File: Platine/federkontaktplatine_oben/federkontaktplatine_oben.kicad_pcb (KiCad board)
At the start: 2 copper layers, 256 x 138 mm, 17 parts, among them J2 Conn_01x08

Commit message: Platinen überarbeitet
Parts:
- added H1: MountingHole, MountingHole:MountingHole_3.2mm_M3_DIN965, F.Cu at (145.5, 105.0)
- added H10: MountingHole, MountingHole:MountingHole_3.2mm_M3_DIN965, F.Cu at (148.0, 38.5)
- added H12: MountingHole, MountingHole:MountingHole_3.2mm_M3_DIN965, F.Cu at (252.5, 80.5)
- added H2: MountingHole, MountingHole:MountingHole_3.2mm_M3_DIN965, F.Cu at (190.5, 50.0)
- added H3: MountingHole, MountingHole:MountingHole_3.2mm_M3_DIN965, F.Cu at (130.5, 50.0)
- added H4: MountingHole, MountingHole:MountingHole_3.2mm_M3_DIN965, F.Cu at (43.5, 39.2)
- added H5: MountingHole, MountingHole:MountingHole_3.2mm_M3_DIN965, F.Cu at (43.5, 119.2)
- added H6: MountingHole, MountingHole:MountingHole_3.2mm_M3_DIN965, F.Cu at (43.5, 80.0)
- added H7: MountingHole, MountingHole:MountingHole_3.2mm_M3_DIN965, F.Cu at (148.0, 125.0)
- added H8: MountingHole, MountingHole:MountingHole_3.2mm_M3_DIN965, F.Cu at (252.5, 39.2)
- added H9: MountingHole, MountingHole:MountingHole_3.2mm_M3_DIN965, F.Cu at (252.5, 119.2)
- added J1: Conn_01x10, Connector_Molex:MOLEX_436501012, F.Cu at (120.0, 120.0)
- added J3: Conn_02x10_Odd_Even, Connector_PinSocket_2.54mm:PinSocket_2x10_P2.54mm_Vertical_SMD, F.Cu at (119.5, 105.0)
- added J4: Conn_02x10_Odd_Even, Connector_PinSocket_2.54mm:PinSocket_2x10_P2.54mm_Vertical_SMD, F.Cu at (169.5, 105.0)
- J2: value Conn_01x08 -> Conn_01x07; footprint Connector_Molex:Molex_Micro-Fit_3.0_43650-0810_1x08-1MP_P3.00mm_Horizontal -> Connector_Molex:MOLEX_436500712
- moved J2 37.8 mm to (170.0, 120.0), turned to 0 degrees
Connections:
- TP1 pad 1: Net-(J2-Pin_1) -> Net-(J4-Pin_15)
- TP10 pad 1: Net-(J2-Pin_6) -> Net-(J4-Pin_5)
- TP11 pad 1: Net-(J2-Pin_7) -> Net-(J4-Pin_3)
- TP12 pad 1: Net-(J2-Pin_7) -> Net-(J4-Pin_3)
- TP13 pad 1: Net-(J2-Pin_8) -> Net-(J4-Pin_1)
- TP14 pad 1: Net-(J2-Pin_8) -> Net-(J4-Pin_1)
- TP15 pad 1: Net-(J2-Pin_4) -> Net-(J4-Pin_9)
- TP16 pad 1: Net-(J2-Pin_4) -> Net-(J4-Pin_9)
- TP2 pad 1: Net-(J2-Pin_1) -> Net-(J4-Pin_15)
- TP3 pad 1: Net-(J2-Pin_2) -> Net-(J4-Pin_13)
- TP4 pad 1: Net-(J2-Pin_2) -> Net-(J4-Pin_13)
- TP5 pad 1: Net-(J2-Pin_3) -> Net-(J4-Pin_11)
- TP6 pad 1: Net-(J2-Pin_3) -> Net-(J4-Pin_11)
- TP7 pad 1: Net-(J2-Pin_5) -> Net-(J4-Pin_7)
- TP8 pad 1: Net-(J2-Pin_5) -> Net-(J4-Pin_7)
- TP9 pad 1: Net-(J2-Pin_6) -> Net-(J4-Pin_5)
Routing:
- net Net-(J4-Pin_7): track 0.00 -> 220.8 mm, vias 0 -> 1
- net Net-(J4-Pin_5): track 0.00 -> 198.0 mm, vias 0 -> 1
- net Net-(J4-Pin_1): track 0.00 -> 191.0 mm, vias 0 -> 1
- net Net-(J4-Pin_3): track 0.00 -> 185.4 mm, vias 0 -> 1
- net Net-(J4-Pin_9): track 0.00 -> 174.2 mm, vias 0 -> 1
- net Net-(J2-Pin_4): track 176.8 -> 14.5 mm, vias 1 -> 0
- net Net-(J2-Pin_5): track 175.8 -> 14.0 mm, vias 1 -> 0
- net Net-(J4-Pin_11): track 0.00 -> 149.2 mm, vias 0 -> 1
- net Net-(J2-Pin_3): track 147.1 -> 13.6 mm, vias 1 -> 0
- net Net-(J2-Pin_6): track 144.6 -> 15.7 mm, vias 1 -> 0
- net Net-(J4-Pin_13): track 0.00 -> 111.0 mm, vias 0 -> 1
- net Net-(J4-Pin_15): track 0.00 -> 96.4 mm, vias 0 -> 1
- net Net-(J2-Pin_2): track 105.5 -> 14.3 mm, vias 1 -> 0
- net Net-(J2-Pin_7): track 105.5 -> 14.3 mm, vias 1 -> 0
- net Net-(J2-Pin_8): track 77.8 -> 0.00 mm, vias 1 -> 0
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- added copper zone on F.Cu, net GND

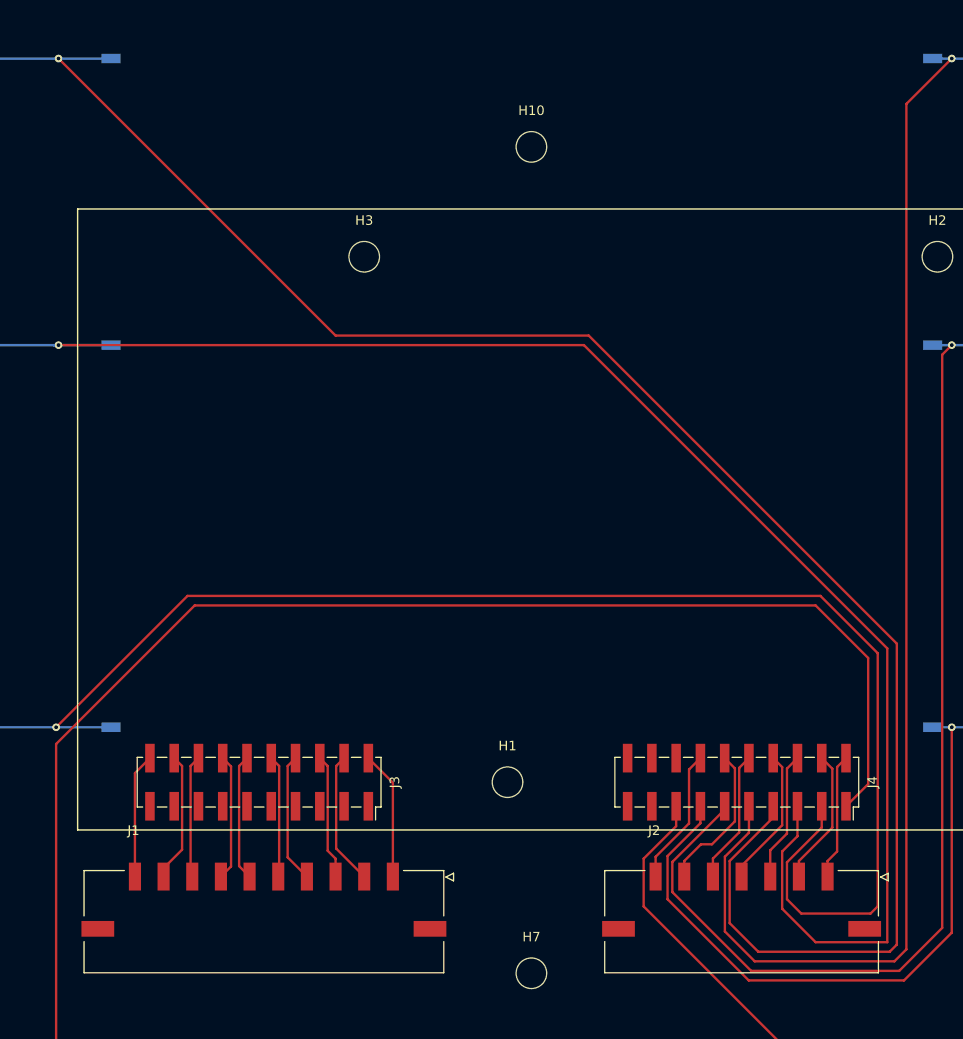
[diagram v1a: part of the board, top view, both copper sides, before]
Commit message: montagelöcher und aufnahme für BMS
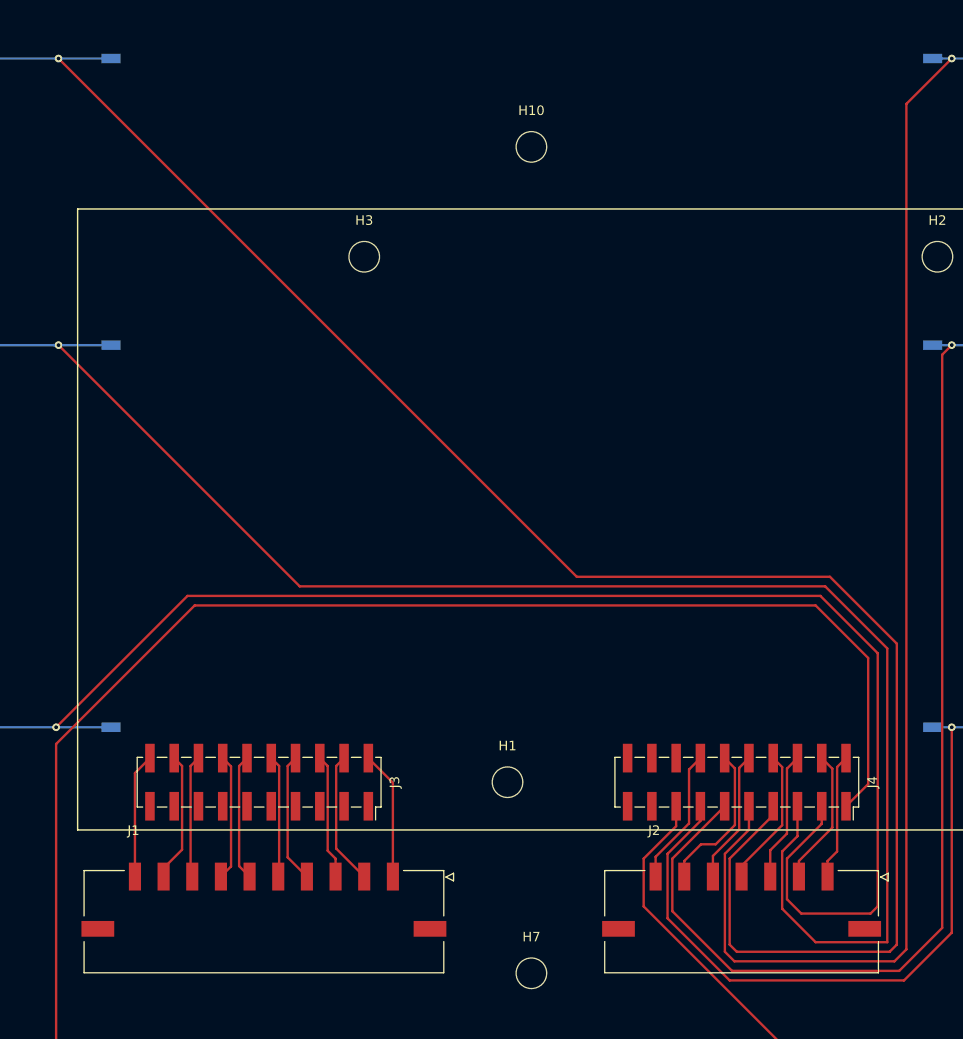
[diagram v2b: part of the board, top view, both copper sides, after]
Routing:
- net Net-(J4-Pin_7): track 220.8 -> 222.1 mm
- net Net-(J4-Pin_9): track 174.2 -> 175.4 mm
- net Net-(J4-Pin_13): track 111.0 -> 112.2 mm
- net Net-(J4-Pin_11): track 149.2 -> 150.4 mm
